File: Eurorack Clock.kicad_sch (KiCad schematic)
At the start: 24 parts, among them J1 Conn_01x10_Pin, J11 Conn_02x08_Row_Letter_Last, J2 Conn_01x08_Pin, U1 ULN2003, U6 L7805

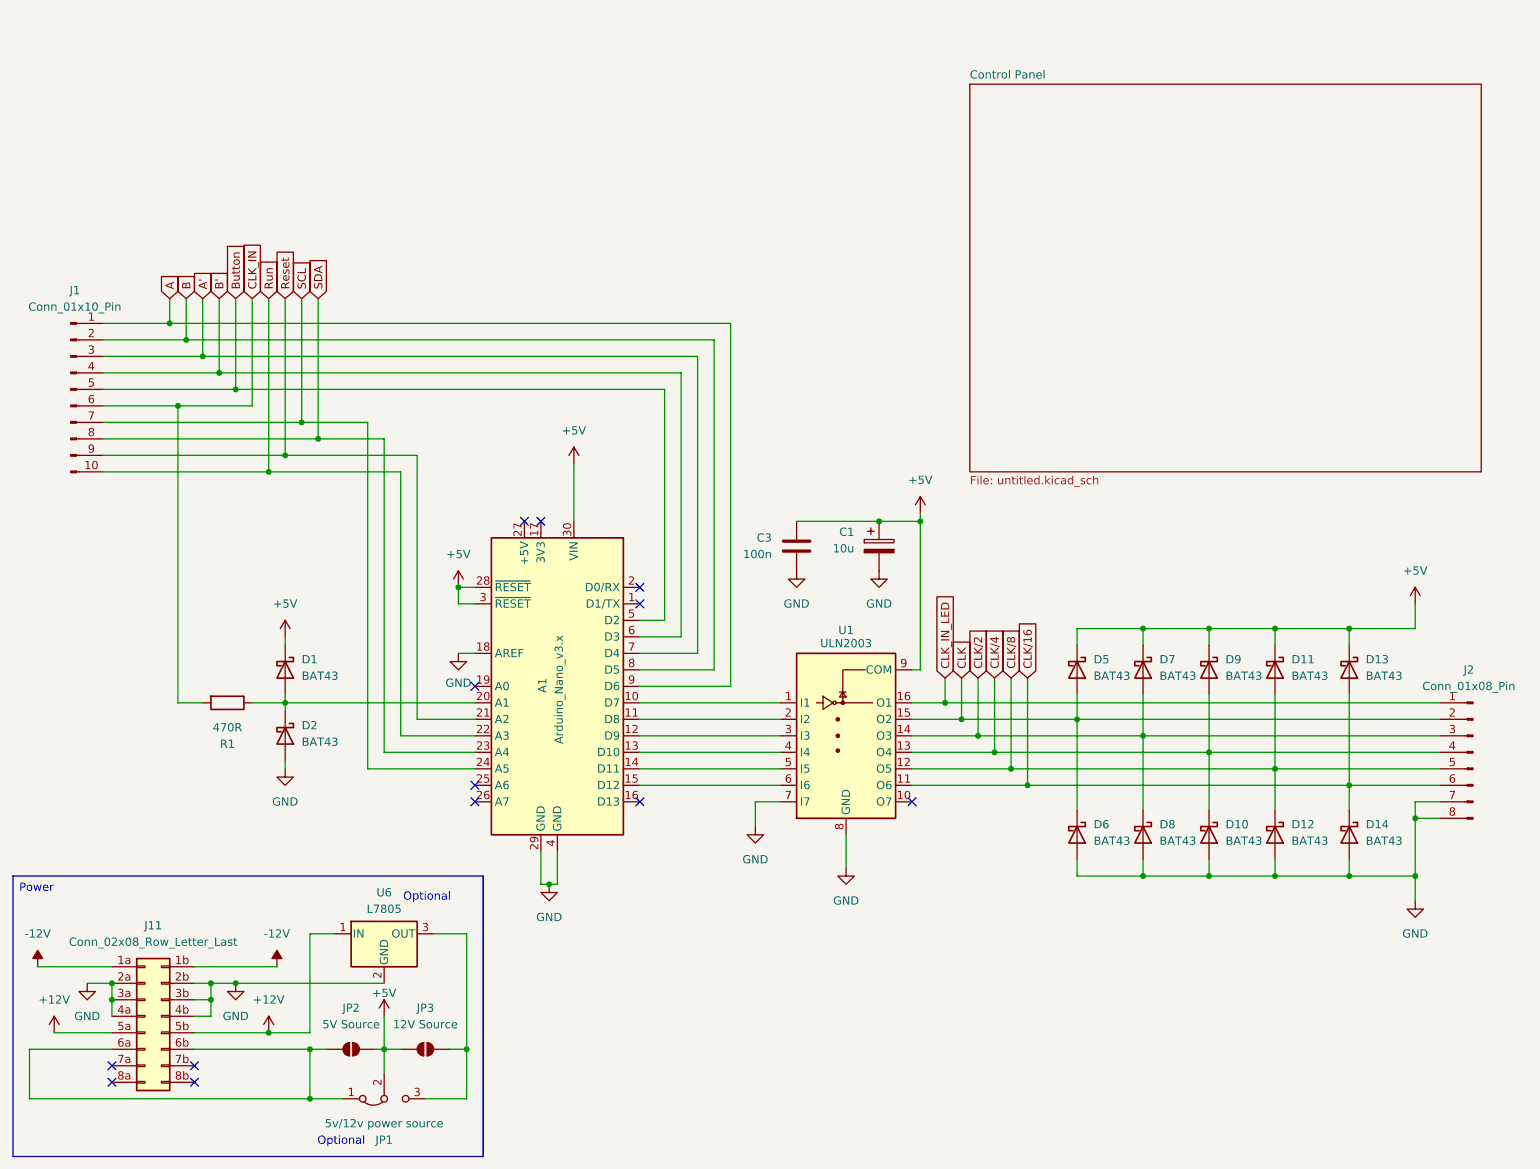
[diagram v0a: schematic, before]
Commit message: Relabeled outputs on schematic and panel, cleaned up pcb layout, removed unused headers, added logo - still need to add to panel
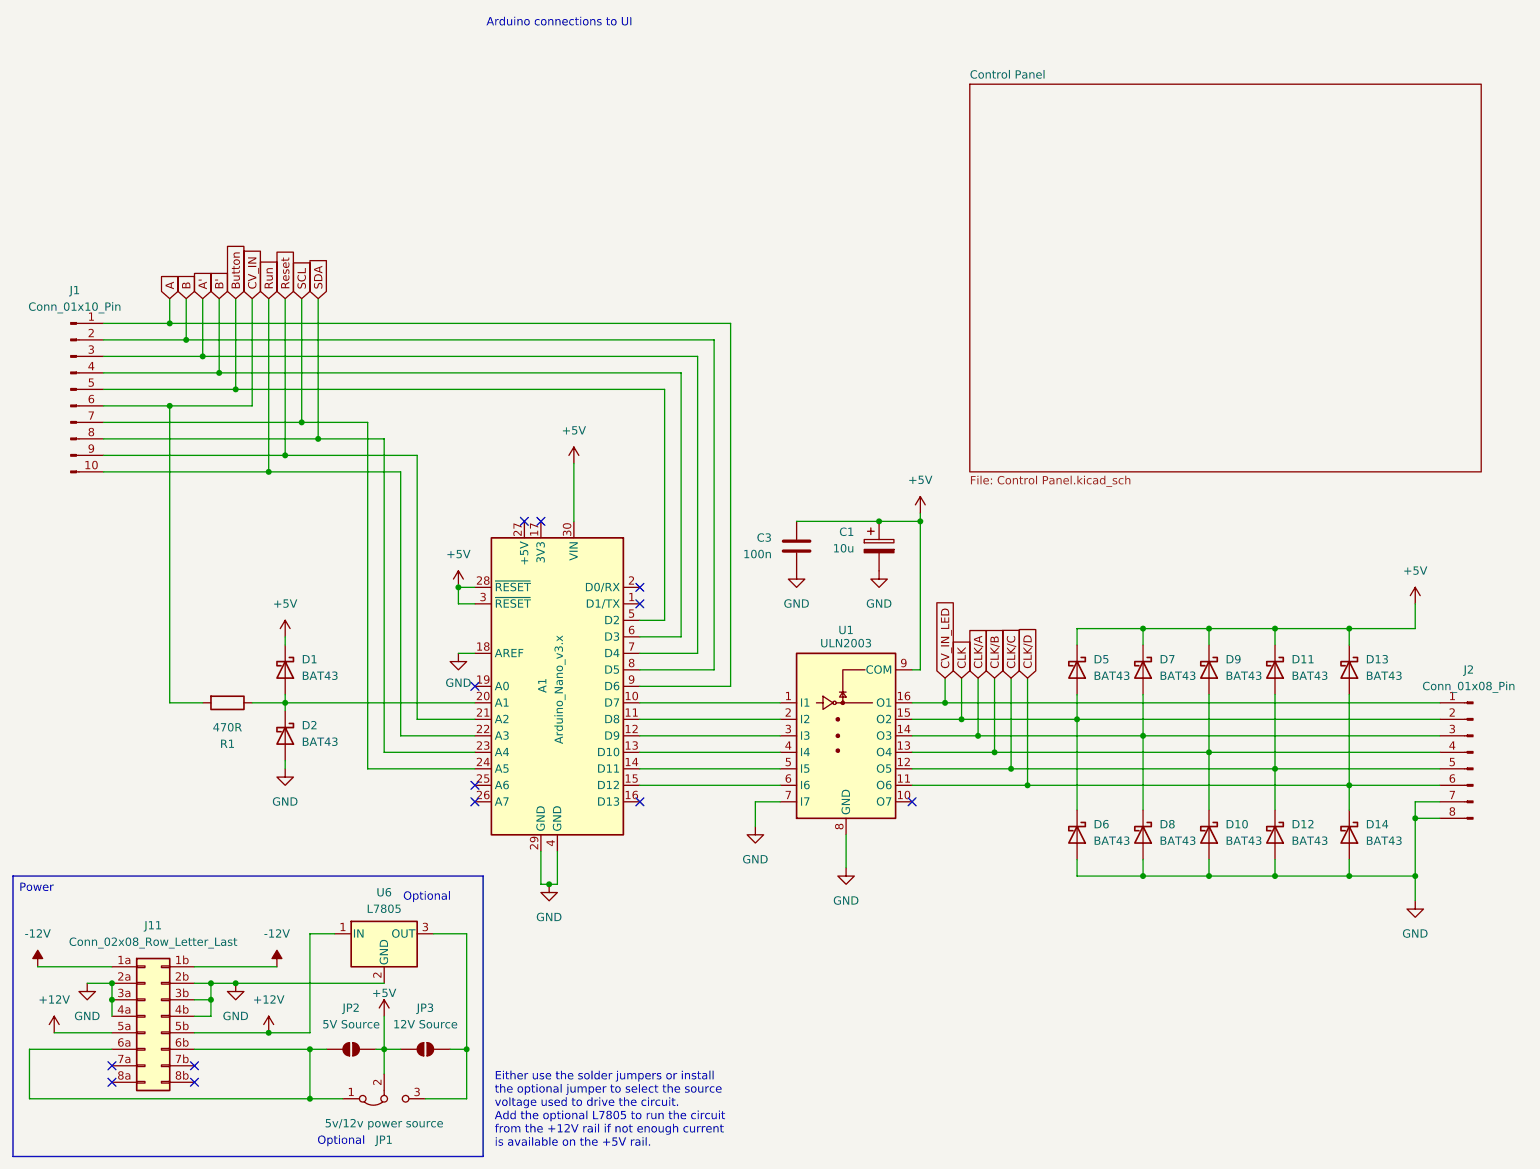
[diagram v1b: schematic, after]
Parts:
- C1: footprint Capacitor_THT:CP_Radial_D10.0mm_P2.50mm -> Capacitor_THT:CP_Radial_D5.0mm_P2.50mm
- C3: footprint (none) -> Capacitor_THT:C_Disc_D4.7mm_W2.5mm_P5.00mm
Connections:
- net CLK_IN renamed CV_IN
- net CLK_IN_LED renamed CV_IN_LED
- net CLK/16 renamed CLK/D
- net CLK/2 renamed CLK/A
- net CLK/4 renamed CLK/B
- net CLK/8 renamed CLK/C
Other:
- sheet Control Panel: file untitled.kicad_sch -> Control Panel.kicad_sch
- note added: "Arduino connections to UI"
- note added: "Either use the solder jumpers or install the optional jumper to select the source voltage used to drive the circuit. Add the optional L7805 to run the circuit from the +12V rail if not enough current is available on the +5V rail."
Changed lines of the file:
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@@
 		)
 	)
+	(text "Either use the solder jumpers or install\nthe optional jumper to select the source \nvoltage used to drive the circuit.\nAdd the optional L7805 to run the circuit\nfrom the +12V rail if not enough current\nis available on the +5V rail."
+		(exclude_from_sim no)
+		(at 91.948 182.118 0)
+		(effects
+			(font
+				(size 1.27 1.27)
+			)
+			(justify left)
+		)
+	)
 	(text "Optional"
 		(exclude_from_sim no)
@@
 		)
 	)
+	(text "Arduino connections to UI"
+		(exclude_from_sim no)
+		(at 90.678 14.732 0)
+		(effects
+			(font
+				(size 1.27 1.27)
+			)
+			(justify left)
+		)
+	)
 	(text_box "Power"
 		(exclude_from_sim no)
@@
 	)
 	(junction
+		(at 41.91 73.66)
+		(diameter 0)
+		(color 0 0 0 0)
+	)
+	(junction
 		(at 191.77 107.95)
 		(diameter 0)
@@
 	)
 	(junction
-		(at 43.18 73.66)
-		(diameter 0)
-		(color 0 0 0 0)
-	)
-	(junction
 		(at 63.5 172.72)
 		(diameter 0)
@@
 	(wire
 		(pts
-			(xy 43.18 73.66) (xy 43.18 119.38)
+			(xy 41.91 73.66) (xy 41.91 119.38)
 		)
 		(stroke
@@
 	(wire
 		(pts
+			(xy 41.91 73.66) (xy 54.61 73.66)
+		)
+		(stroke
+			(width 0)
+			(type default)
+		)
+	)
+	(wire
+		(pts
 			(xy 48.26 162.56) (xy 48.26 165.1)
 		)
@@
 	(wire
 		(pts
-			(xy 31.75 73.66) (xy 43.18 73.66)
+			(xy 31.75 73.66) (xy 41.91 73.66)
 		)
 		(stroke
@@
 	(wire
 		(pts
-			(xy 43.18 73.66) (xy 54.61 73.66)
-		)
-		(stroke
-			(width 0)
-			(type default)
-		)
-	)
-	(wire
-		(pts
 			(xy 191.77 107.95) (xy 201.93 107.95)
 		)
@@
 	(wire
 		(pts
-			(xy 43.18 119.38) (xy 46.99 119.38)
+			(xy 41.91 119.38) (xy 46.99 119.38)
 		)
 		(stroke
@@
 		)
 	)
-	(global_label "CLK_IN"
+	(global_label "CV_IN"
 		(shape input)
 		(at 54.61 57.15 90)
@@
 		)
 		(property "Intersheetrefs" "${INTERSHEET_REFS}"
-			(at 54.61 47.6938 90)
+			(at 54.61 48.9033 90)
 			(effects
 				(font
@@
 		)
 	)
-	(global_label "CLK{slash}16"
+	(global_label "CLK{slash}D"
 		(shape input)
 		(at 173.99 115.57 90)
@@
 		)
 		(property "Intersheetrefs" "${INTERSHEET_REFS}"
-			(at 173.99 105.2672 90)
+			(at 173.99 106.4162 90)
 			(effects
 				(font
@@
 		)
 	)
-	(global_label "CLK{slash}2"
+	(global_label "CLK{slash}A"
 		(shape input)
 		(at 166.37 115.57 90)
@@
 		)
 		(property "Intersheetrefs" "${INTERSHEET_REFS}"
-			(at 166.37 106.4767 90)
+			(at 166.37 106.5976 90)
 			(effects
 				(font
@@
 		)
 	)
-	(global_label "CLK{slash}4"
+	(global_label "CLK{slash}B"
 		(shape input)
 		(at 168.91 115.57 90)
@@
 		)
 		(property "Intersheetrefs" "${INTERSHEET_REFS}"
-			(at 168.91 106.4767 90)
+			(at 168.91 106.4162 90)
 			(effects
 				(font
@@
 		)
 	)
-	(global_label "CLK_IN_LED"
+	(global_label "CV_IN_LED"
 		(shape input)
 		(at 161.29 115.57 90)
@@
 		)
 		(property "Intersheetrefs" "${INTERSHEET_REFS}"
-			(at 161.29 101.6991 90)
+			(at 161.29 102.9086 90)
 			(effects
 				(font
@@
 		)
 	)
-	(global_label "CLK{slash}8"
+	(global_label "CLK{slash}C"
 		(shape input)
 		(at 171.45 115.57 90)
@@
 		)
 		(property "Intersheetrefs" "${INTERSHEET_REFS}"
-			(at 171.45 106.4767 90)
+			(at 171.45 106.4162 90)
 			(effects
 				(font
@@
 	(hierarchical_label ""
 		(shape input)
-		(at 74.93 44.45 0)
-		(effects
-			(font
-				(size 1.27 1.27)
-			)
-			(justify left)
-		)
-	)
-	(hierarchical_label ""
-		(shape input)
 		(at 165.1 53.34 0)
 		(effects
@@
 	(hierarchical_label ""
 		(shape input)
-		(at 80.01 31.75 0)
-		(effects
-			(font
-				(size 1.27 1.27)
-			)
-			(justify left)
-		)
-	)
-	(hierarchical_label ""
-		(shape input)
 		(at 165.1 53.34 0)
 		(effects
@@
 	(hierarchical_label ""
 		(shape input)
-		(at 74.93 44.45 0)
-		(effects
-			(font
-				(size 1.27 1.27)
-			)
-			(justify left)
-		)
-	)
-	(hierarchical_label ""
-		(shape input)
 		(at 165.1 53.34 0)
 		(effects
@@
 	(hierarchical_label ""
 		(shape input)
-		(at 76.2 59.69 0)
-		(effects
-			(font
-				(size 1.27 1.27)
-			)
-			(justify left)
-		)
-	)
-	(hierarchical_label ""
-		(shape input)
 		(at 165.1 53.34 0)
 		(effects
@@
 			)
 		)
-		(property "Footprint" "Capacitor_THT:CP_Radial_D10.0mm_P2.50mm"
+		(property "Footprint" "Capacitor_THT:CP_Radial_D5.0mm_P2.50mm"
 			(at 152.0952 99.06 0)
 			(effects
@@
 			)
 		)
-		(property "Footprint" ""
+		(property "Footprint" "Capacitor_THT:C_Disc_D4.7mm_W2.5mm_P5.00mm"
 			(at 137.4648 99.06 0)
 			(effects
@@
 			)
 		)
-		(property "Sheetfile" "untitled.kicad_sch"
+		(property "Sheetfile" "Control Panel.kicad_sch"
 			(at 165.1 84.4046 0)
 			(effects
